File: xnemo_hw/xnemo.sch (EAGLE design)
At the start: 25 parts, among them J1 MICRO_USB_B_RECEPT, J2 DM3D_MICRO_SD, J3 HEADER_2X5, U1 LTC3559, U2 L3GD20, U3 STM32F405RG, U5 HMC5883L, U6 ADXL345, X1 TXC_7A_XTAL

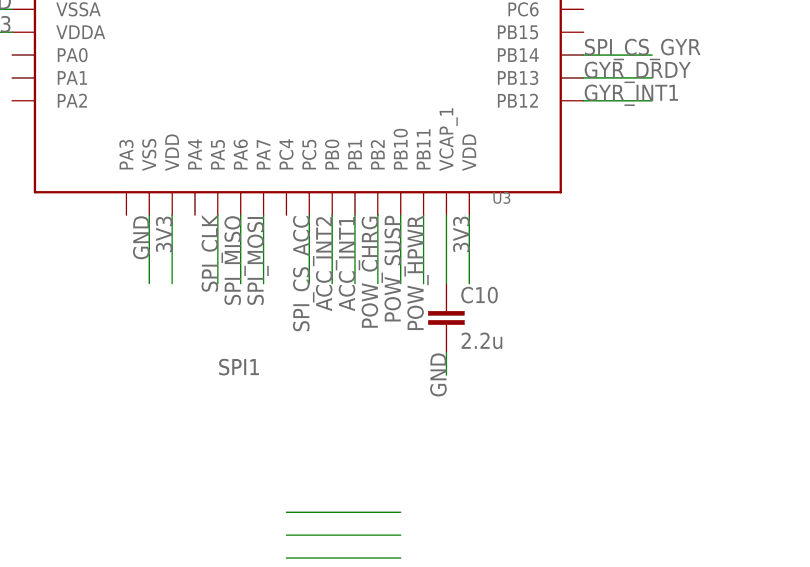
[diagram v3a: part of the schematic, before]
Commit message: Most of the PCB is routed
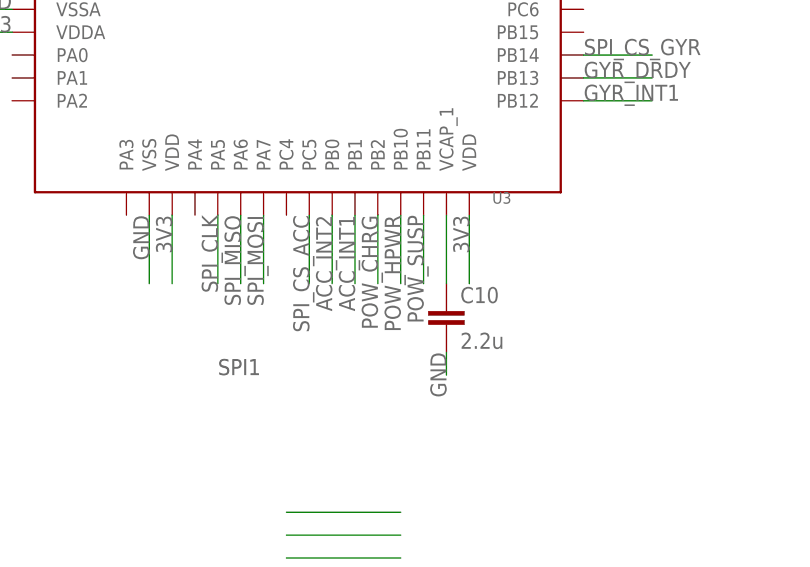
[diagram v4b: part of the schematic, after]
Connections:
- net N$17 renamed VCAP_1
- net N$5 renamed VCAP_2
- net POW_HPWR: now also U3.PB10; no longer U3.PB11
- net POW_SUSP: now also U3.PB11; no longer U3.PB10
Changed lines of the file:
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@@
+</segment>
+<segment>
+<pinref part="U3" gate="G$1" pin="PB11"/>
+<wire x1="43.18" y1="-7.62" x2="43.18" y2="-15.24" width="0.1524" layer="91"/>
+<label x="43.18" y="-7.62" size="1.778" layer="95" rot="MR270"/>
+</segment>
+</net>
+<net name="POW_HPWR" class="0">
+<segment>
+<pinref part="U1" gate="G$1" pin="HPWR"/>
+<wire x1="-38.1" y1="86.36" x2="-27.94" y2="86.36" width="0.1524" layer="91"/>
+<label x="-38.1" y="86.36" size="1.778" layer="95"/>
 </segment>
 <segment>
@@
 <wire x1="40.64" y1="-7.62" x2="40.64" y2="-15.24" width="0.1524" layer="91"/>
 <label x="40.64" y="-7.62" size="1.778" layer="95" rot="MR270"/>
-</segment>
-</net>
-<net name="POW_HPWR" class="0">
-<segment>
-<pinref part="U1" gate="G$1" pin="HPWR"/>
-<wire x1="-38.1" y1="86.36" x2="-27.94" y2="86.36" width="0.1524" layer="91"/>
-<label x="-38.1" y="86.36" size="1.778" layer="95"/>
-</segment>
-<segment>
-<pinref part="U3" gate="G$1" pin="PB11"/>
-<wire x1="43.18" y1="-7.62" x2="43.18" y2="-15.24" width="0.1524" layer="91"/>
-<label x="43.18" y="-7.62" size="1.778" layer="95" rot="MR270"/>
 </segment>
 </net>
@@
 </segment>
 </net>
-<net name="N$5" class="0">
+<net name="VCAP_2" class="0">
 <segment>
 <pinref part="U3" gate="G$1" pin="VCAP_2"/>
@@
 </segment>
 </net>
-<net name="N$17" class="0">
+<net name="VCAP_1" class="0">
 <segment>
 <pinref part="C10" gate="G$1" pin="1"/>

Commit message: Mostly routed!
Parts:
- added C13: 100n, resistor:C-EUC0402
- added J4, J5: HEADER_2X5, xnemo:HEADER_2X5
- added R5, R6: 22k, resistor:R-US_R0402
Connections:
- net N$1 renamed POW_PROG
- removed net JNTRST: U3.PB4
- new net N$1: J5.4
- new net N$15: J4.10
- new net N$16: J5.7
- new net N$17: J5.5
- new net N$2: J5.2
- new net N$3: J5.3
- new net N$4: J5.1
- new net N$5: J5.6
- new net N$6: J5.8
- new net N$7: J4.9
- new net N$8: J5.10
- new net N$9: J5.9
- new net PA0: J4.6, U3.PA0
- new net PA1: J4.5, U3.PA1
- new net PA2: J4.2, U3.PA2
- new net PA3: J4.1, U3.PA3
- new net PA4: J4.8, U3.PA4
- new net PC0: U3.PC0
- new net PC1: U3.PC1
- new net PC2: U3.PC2
- new net PC3: U3.PC3
- new net PC4: J4.7, U3.PC4
- net 3V3: now also C13.1, J4.4, R5.2, R6.2
- net GND: now also C13.2, J4.3, U1.EN2, U3.B00T0
- net I2C_SCL: now also R6.1
- net I2C_SDA: now also R5.1
- net MAG_DRDY: now also U3.PB8
- net SD_DET: now also U3.PB4

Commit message: Passes DRC
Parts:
- added C14: 22p, resistor:C-EUC0402
- C7: value 10u -> 1u; device resistor:C-EUC0805 -> resistor:C-EUC0603
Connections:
- removed net N$15: J4.10
- net 3V3: now also C14.2
- net BUCK_FB1: now also C14.1
- net GND: now also U5.GND@2
- net PA0: now also J4.8; no longer J4.6
- net PA1: now also J4.6
- net PA4: now also J4.10; no longer J4.8
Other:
- moved on the sheet: C6

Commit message: Expansion headers are now thru-hole
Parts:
- removed C13: 100n, resistor:C-EUC0402
- added C15: 220n, resistor:C-EUC0402
- added C16, C17: 10u, resistor:C-EUC0805
- added C18: 100n, resistor:C-EUC0402
- C1: value (none) -> 10n
- C8: value 2.2u -> 4.7u
- J3: value HEADER_2X5 -> HEADER_2X5_0.05_SMD; device xnemo:HEADER_2X5 -> xnemo:HEADER_2X5_0.05_SMD
- J4, J5: value HEADER_2X5 -> HEADER_2X5_0.05_THRU; device xnemo:HEADER_2X5 -> xnemo:HEADER_2X5_0.05_THRU
- R3: value (none) -> 1.74k
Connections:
- net 3V3: now also C15.2, C16.1, C17.1, C18.2; no longer C13.1
- net GND: now also C15.1, C16.2, C17.2, C18.1; no longer C13.2
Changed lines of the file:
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@@
 <part name="U6" library="xnemo" deviceset="ADXL345" device=""/>
 <part name="L1" library="xnemo" deviceset="NR4018" device=""/>
-<part name="C1" library="resistor" deviceset="C-EU" device="C0402"/>
+<part name="C1" library="resistor" deviceset="C-EU" device="C0402" value="10n"/>
 <part name="C2" library="resistor" deviceset="C-EU" device="C0402" value="0.22u"/>
 <part name="C3" library="resistor" deviceset="C-EU" device="C0805" value="4.7u"/>
@@
 <part name="R2" library="resistor" deviceset="R-US_" device="R0402"/>
 <part name="C7" library="resistor" deviceset="C-EU" device="C0603" value="1u"/>
-<part name="C8" library="resistor" deviceset="C-EU" device="C0805" value="2.2u"/>
-<part name="R3" library="resistor" deviceset="R-US_" device="R0402"/>
+<part name="C8" library="resistor" deviceset="C-EU" device="C0805" value="4.7u"/>
+<part name="R3" library="resistor" deviceset="R-US_" device="R0402" value="1.74k"/>
 <part name="J2" library="xnemo" deviceset="DM3D_MICRO_SD" device=""/>
-<part name="J3" library="xnemo" deviceset="HEADER_2X5" device=""/>
+<part name="J3" library="xnemo" deviceset="HEADER_2X5" device="_0.05_SMD"/>
 <part name="U2" library="xnemo" deviceset="L3GD20" device=""/>
 <part name="C9" library="resistor" deviceset="C-EU" device="C0603" value="2.2u"/>
@@
 <part name="C11" library="resistor" deviceset="C-EU" device="C0603" value="2.2u"/>
 <part name="C12" library="resistor" deviceset="C-EU" device="C0603" value="2.2u"/>
-<part name="C13" library="resistor" deviceset="C-EU" device="C0402" value="100n"/>
-<part name="J4" library="xnemo" deviceset="HEADER_2X5" device=""/>
-<part name="J5" library="xnemo" deviceset="HEADER_2X5" device=""/>
+<part name="J4" library="xnemo" deviceset="HEADER_2X5" device="_0.05_THRU"/>
+<part name="J5" library="xnemo" deviceset="HEADER_2X5" device="_0.05_THRU"/>
 <part name="R5" library="resistor" deviceset="R-US_" device="R0402" value="22k"/>
 <part name="R6" library="resistor" deviceset="R-US_" device="R0402" value="22k"/>
 <part name="C14" library="resistor" deviceset="C-EU" device="C0402" value="22p"/>
+<part name="C15" library="resistor" deviceset="C-EU" device="C0402" value="220n"/>
+<part name="C16" library="resistor" deviceset="C-EU" device="C0805" value="10u"/>
+<part name="C17" library="resistor" deviceset="C-EU" device="C0805" value="10u"/>
+<part name="C18" library="resistor" deviceset="C-EU" device="C0402" value="100n"/>
 </parts>
 <sheets>
@@
 <instance part="C11" gate="G$1" x="71.12" y="40.64" rot="R90"/>
 <instance part="C12" gate="G$1" x="10.16" y="66.04" rot="R90"/>
-<instance part="C13" gate="G$1" x="109.22" y="-33.02" rot="R180"/>
 <instance part="J4" gate="G$1" x="22.86" y="-45.72"/>
 <instance part="J5" gate="G$1" x="-15.24" y="-43.18"/>
@@
 <instance part="R6" gate="G$1" x="25.4" y="86.36" rot="R90"/>
 <instance part="C14" gate="G$1" x="-76.2" y="55.88" rot="R90"/>
+<instance part="C15" gate="G$1" x="96.52" y="93.98"/>
+<instance part="C16" gate="G$1" x="88.9" y="91.44" rot="R180"/>
+<instance part="C17" gate="G$1" x="109.22" y="-33.02" rot="R180"/>
+<instance part="C18" gate="G$1" x="104.14" y="-22.86" rot="R90"/>
 </instances>
 <busses>
@@
 <wire x1="88.9" y1="68.58" x2="86.36" y2="68.58" width="0.1524" layer="91"/>
 <wire x1="86.36" y1="68.58" x2="86.36" y2="83.82" width="0.1524" layer="91"/>
-<wire x1="86.36" y1="83.82" x2="101.6" y2="83.82" width="0.1524" layer="91"/>
+<wire x1="86.36" y1="83.82" x2="88.9" y2="83.82" width="0.1524" layer="91"/>
+<wire x1="88.9" y1="83.82" x2="96.52" y2="83.82" width="0.1524" layer="91"/>
+<wire x1="96.52" y1="83.82" x2="101.6" y2="83.82" width="0.1524" layer="91"/>
 <wire x1="104.14" y1="83.82" x2="101.6" y2="83.82" width="0.1524" layer="91"/>
 <label x="91.44" y="83.82" size="1.778" layer="95"/>
@@
 <pinref part="U2" gate="G$1" pin="VDD"/>
 <junction x="101.6" y="83.82"/>
+<pinref part="C16" gate="G$1" pin="1"/>
+<wire x1="88.9" y1="88.9" x2="88.9" y2="83.82" width="0.1524" layer="91"/>
+<pinref part="C15" gate="G$1" pin="2"/>
+<wire x1="96.52" y1="88.9" x2="96.52" y2="83.82" width="0.1524" layer="91"/>
 </segment>
 <segment>
@@
 <wire x1="119.38" y1="-35.56" x2="109.22" y2="-35.56" width="0.1524" layer="91"/>
 <label x="119.38" y="-35.56" size="1.778" layer="95" rot="MR0"/>
-<pinref part="C13" gate="G$1" pin="1"/>
+<pinref part="C17" gate="G$1" pin="1"/>
 </segment>
 <segment>
 <pinref part="U6" gate="G$1" pin="VDDIO"/>
-<wire x1="119.38" y1="-22.86" x2="111.76" y2="-22.86" width="0.1524" layer="91"/>
+<wire x1="119.38" y1="-22.86" x2="109.22" y2="-22.86" width="0.1524" layer="91"/>
 <label x="119.38" y="-22.86" size="1.778" layer="95" rot="MR0"/>
+<pinref part="C18" gate="G$1" pin="2"/>
 </segment>
 <segment>
@@
 <wire x1="121.92" y1="63.5" x2="127" y2="63.5" width="0.1524" layer="91"/>
 <wire x1="121.92" y1="66.04" x2="127" y2="66.04" width="0.1524" layer="91"/>
-<wire x1="109.22" y1="83.82" x2="127" y2="83.82" width="0.1524" layer="91"/>
+<wire x1="109.22" y1="83.82" x2="116.84" y2="83.82" width="0.1524" layer="91"/>
+<wire x1="116.84" y1="83.82" x2="127" y2="83.82" width="0.1524" layer="91"/>
 <wire x1="127" y1="83.82" x2="127" y2="68.58" width="0.1524" layer="91"/>
 <wire x1="111.76" y1="88.9" x2="109.22" y2="88.9" width="0.1524" layer="91"/>
@@
 <junction x="127" y="63.5"/>
 <junction x="127" y="60.96"/>
+<pinref part="C16" gate="G$1" pin="2"/>
+<wire x1="88.9" y1="96.52" x2="88.9" y2="99.06" width="0.1524" layer="91"/>
+<wire x1="88.9" y1="99.06" x2="96.52" y2="99.06" width="0.1524" layer="91"/>
+<pinref part="C15" gate="G$1" pin="1"/>
+<wire x1="96.52" y1="99.06" x2="96.52" y2="96.52" width="0.1524" layer="91"/>
+<wire x1="96.52" y1="99.06" x2="116.84" y2="99.06" width="0.1524" layer="91"/>
+<wire x1="116.84" y1="99.06" x2="116.84" y2="83.82" width="0.1524" layer="91"/>
+<junction x="116.84" y="83.82"/>
+<junction x="96.52" y="99.06"/>
 </segment>
 <segment>
@@
 <wire x1="119.38" y1="-25.4" x2="111.76" y2="-25.4" width="0.1524" layer="91"/>
 <wire x1="111.76" y1="-30.48" x2="111.76" y2="-27.94" width="0.1524" layer="91"/>
-<pinref part="C13" gate="G$1" pin="2"/>
 <wire x1="111.76" y1="-27.94" x2="111.76" y2="-25.4" width="0.1524" layer="91"/>
 <wire x1="109.22" y1="-27.94" x2="111.76" y2="-27.94" width="0.1524" layer="91"/>
 <junction x="111.76" y="-30.48"/>
 <junction x="111.76" y="-27.94"/>
+<pinref part="C17" gate="G$1" pin="2"/>
+<pinref part="C18" gate="G$1" pin="1"/>
+<wire x1="101.6" y1="-22.86" x2="99.06" y2="-22.86" width="0.1524" layer="91"/>
+<wire x1="99.06" y1="-22.86" x2="99.06" y2="-27.94" width="0.1524" layer="91"/>
+<wire x1="99.06" y1="-27.94" x2="109.22" y2="-27.94" width="0.1524" layer="91"/>
 </segment>
 <segment>
@@
 <segment>
 <wire x1="101.6" y1="48.26" x2="101.6" y2="43.18" width="0.1524" layer="91"/>
-<label x="101.6" y="48.26" size="1.778" layer="95" rot="R180"/>
+<label x="101.6" y="48.26" size="1.778" layer="95" rot="MR270"/>
 <pinref part="U2" gate="G$1" pin="CS"/>
 </segment>
@@
 <pinref part="J4" gate="G$1" pin="6"/>
 <wire x1="17.78" y1="-45.72" x2="5.08" y2="-45.72" width="0.1524" layer="91"/>
+<label x="17.78" y="-45.72" size="1.778" layer="95" rot="MR0"/>
 </segment>
 </net>
@@
 <pinref part="J4" gate="G$1" pin="8"/>
 <wire x1="17.78" y1="-48.26" x2="5.08" y2="-48.26" width="0.1524" layer="91"/>
+<label x="17.78" y="-48.26" size="1.778" layer="95" rot="MR0"/>
 </segment>
 </net>
@@
 <pinref part="J4" gate="G$1" pin="10"/>
 <wire x1="17.78" y1="-50.8" x2="5.08" y2="-50.8" width="0.1524" layer="91"/>
-</segment>
-</net>
+<label x="17.78" y="-50.8" size="1.778" layer="95" rot="MR0"/>
+</segment>
+</net>

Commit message: r1 submitted
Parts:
- added C13: 2.2u, resistor:C-EUC0603
- added J6: (no value), pinhead:PINHD-1X2
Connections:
- removed net N$1: J5.4
- removed net N$16: J5.7
- removed net N$17: J5.5
- removed net N$2: J5.2
- removed net N$3: J5.3
- removed net N$4: J5.1
- removed net N$5: J5.6
- removed net N$6: J5.8
- removed net N$7: J4.9
- removed net N$8: J5.10
- removed net N$9: J5.9
- new net PA10: U3.PA10
- new net PB12: J5.9, U3.PB12
- new net PB13: J5.10, U3.PB13
- new net PB14: J5.4, U3.PB14
- new net PB15: J5.6, U3.PB15
- new net PC13: J5.1, U3.PC13
- new net UC_VBAT: C13.2, U3.VBAT
- net 3V3: now also C13.1, J5.2, J5.8
- net GND: now also J5.3, J5.5, J5.7, J6.1
- net GYR_DRDY: now also U3.PC7; no longer U3.PB13
- net GYR_INT1: now also U3.PC6; no longer U3.PB12
- net I2C_SCL: now also J4.5
- net I2C_SDA: now also J4.9
- net PA1: no longer J4.5
- net SPI_CS_GYR: now also U3.PA8; no longer U3.PB14
- net VBAT: now also J6.2
